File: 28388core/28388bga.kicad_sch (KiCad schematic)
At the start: 131 parts, among them IC1 F28388DZWTS, IC2 TPS62420DRCT, IC6 OPA4350EA_250, IC7 TPS3702CX33DDCT, IC8 CDCLVC1104PW, J4 Conn_02x10_Top_Bottom, J6 2.54-2*5, J9 Conn_02x07_Odd_Even, M1 Conn_01x01_Socket, M2 Conn_01x01_Socket, M3 Conn_01x01_Socket, M4 Conn_01x01_Socket, M5 Conn_01x01_Socket, M6 Conn_01x01_Socket, M7 Conn_01x01_Socket, Q1 FMMT618TA, Q11 AT24C16C-SSHM-T, Q2 FMMT618TA, Q4 FMMT618TA, Q7 FMMT618TA, SW1 SW_DIP_x02, SW2 SW_Push, U1 ADR423ARMZ, Y1 ECS-2520S33-250-FN-TR

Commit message: 第一版引脚分配
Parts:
- removed C216, C218: 0.1uF/50V, Capacitor_SMD:C_0603_1608Metric, symbol sheet1-altium-import:CAP_2
- removed C217, C219: 10uF/50V, Capacitor_SMD:C_0603_1608Metric, symbol sheet1-altium-import:CAP_2
- removed J4: Conn_02x10_Top_Bottom, Connector_PinHeader_2.54mm:PinHeader_2x10_P2.54mm_Vertical, symbol Connector_Generic:Conn_02x10_Top_Bottom
- removed M1, M2, M3, M4, M5, M6, M7: Conn_01x01_Socket, 1mmlab_footprint:M3, symbol Connector:Conn_01x01_Socket
- added CARD2: DDR3, 1mmlab_footprint:PCBComponent_1 - duplicate, symbol 1mmlab:DDR3
- added D45: SK36A-LTP, Lib_sheet_10:SMA_L4.3-W2.6-LS5.2-RD, symbol sheet1-altium-import:SK36A-LTP
- added H1, H2: MountingHole_Pad, MountingHole:MountingHole_2.2mm_M2_Pad_Via, symbol Mechanical:MountingHole_Pad
- added Q46: TYPEC-304-ACP16, Lib4:USB-C-SMD_TYPE-C-16P-1, symbol sheet1-altium-import:TYPEC-304-ACP16
- added R301, R302: 4.7K/1%, Resistor_SMD:R_0603_1608Metric, symbol sheet1-altium-import:RES_4
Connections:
- net ADC_14_IN: now also CARD2.19
- net ADC_15_IN: now also CARD2.21
- net ADC_A0_IN: now also CARD2.3
- net ADC_A1_IN: now also CARD2.5
- net ADC_A2_IN: now also CARD2.9
- net ADC_A3_IN: now also CARD2.11
- net ADC_A4_IN: now also CARD2.15
- net ADC_A5_IN: now also CARD2.17
- net ADC_B0_IN: now also CARD2.4
- net ADC_B1_IN: now also CARD2.6
- net ADC_B2_IN: now also CARD2.10
- net ADC_B3_IN: now also CARD2.12
- net ADC_B4_IN: now also CARD2.16
- net ADC_B5_IN: now also CARD2.18
- net ADC_C2_IN: now also CARD2.25
- net ADC_C3_IN: now also CARD2.27
- net ADC_C4_IN: now also CARD2.31
- net ADC_C5_IN: now also CARD2.33
- net ADC_D0_IN: now also CARD2.20
- net ADC_D1_IN: now also CARD2.22
- net ADC_D2_IN: now also CARD2.26
- net ADC_D3_IN: now also CARD2.28
- net ADC_D4_IN: now also CARD2.32
- net ADC_D5_IN: now also CARD2.34
- net D+5V: now also D45.1 (K)
- net DSP_GPIO145: now also D10.2 (K), R39.2
- net DSP_GPIO146: now also D11.1 (K), R40.2
- net DSP_GPIO150: now also Q11.5 (SDA), R34.1
- net DSP_GPIO151: now also Q11.6 (SCL), R33.1
- net DSP_GPIO40: no longer Q11.5 (SDA), R34.1
- net DSP_GPIO41: no longer Q11.6 (SCL), R33.1
- net DSP_GPIO60: no longer D10.2 (K), R39.2
- net DSP_GPIO61: no longer D11.1 (K), R40.2
- net PE_GND: now also H1.1, H2.1
- new net: Q46.B5 (CC2), R302.2
- new net: Q46.A5 (CC1), R301.1
- new net AGND: Q46.A1B12 (GND), Q46.B1A12 (GND), R301.2, R302.1
- new net GPIO0: CARD2.47
- new net GPIO1: CARD2.49
- new net GPIO10: CARD2.61
- new net GPIO100: CARD2.173
- new net GPIO101: CARD2.175
- new net GPIO102: CARD2.166
- new net GPIO103: CARD2.168
- new net GPIO104: CARD2.170
- new net GPIO105: CARD2.172
- new net GPIO106: CARD2.174
- new net GPIO107: CARD2.176
- new net GPIO108: CARD2.179
- new net GPIO109: CARD2.181
- new net GPIO11: CARD2.63
- new net GPIO110: CARD2.183
- new net GPIO111: CARD2.185
- new net GPIO112: CARD2.187
- new net GPIO115: CARD2.180
- new net GPIO116: CARD2.182
- new net GPIO117: CARD2.184
- new net GPIO119: CARD2.186
- new net GPIO12: CARD2.58
- new net GPIO120: CARD2.188
- new net GPIO121: CARD2.191
- new net GPIO122: CARD2.193
- new net GPIO123: CARD2.195
- new net GPIO124: CARD2.197
- new net GPIO126: CARD2.192
- new net GPIO127: CARD2.194
- new net GPIO128: CARD2.196
- new net GPIO13: CARD2.60
- new net GPIO14: CARD2.62
- new net GPIO147: CARD2.198
- new net GPIO15: CARD2.64
- new net GPIO154: CARD2.200
- new net GPIO16: CARD2.67
- new net GPIO17: CARD2.69
- new net GPIO18: CARD2.68
- new net GPIO19: CARD2.70
- new net GPIO2: CARD2.51
- new net GPIO20: CARD2.77
- new net GPIO21: CARD2.79
- new net GPIO22: CARD2.81
- new net GPIO23: CARD2.83
- new net GPIO24: CARD2.85
- new net GPIO25: CARD2.87
- new net GPIO26: CARD2.78
- new net GPIO27: CARD2.80
- new net GPIO28: CARD2.82
- new net GPIO29: CARD2.84
- new net GPIO3: CARD2.53
- new net GPIO30: CARD2.86
- new net GPIO31: CARD2.88
- new net GPIO32: CARD2.91
- new net GPIO33: CARD2.93
- new net GPIO34: CARD2.95
- new net GPIO35: CARD2.97
- new net GPIO36: CARD2.99
- new net GPIO37: CARD2.101
- new net GPIO38: CARD2.92
- new net GPIO39: CARD2.94
- new net GPIO4: CARD2.48
- new net GPIO40: CARD2.96
- new net GPIO41: CARD2.98
- new net GPIO42: CARD2.100
- new net GPIO43: CARD2.102
- new net GPIO44: CARD2.105
- new net GPIO45: CARD2.107
- new net GPIO46: CARD2.109
- new net GPIO47: CARD2.111
- new net GPIO48: CARD2.113
- new net GPIO49: CARD2.115
- new net GPIO5: CARD2.50
- new net GPIO50: CARD2.106
- new net GPIO51: CARD2.108
- new net GPIO52: CARD2.110
- new net GPIO53: CARD2.112
- new net GPIO54: CARD2.114
- new net GPIO55: CARD2.116
- new net GPIO56: CARD2.119
- new net GPIO57: CARD2.121
- new net GPIO58: CARD2.123
- new net GPIO59: CARD2.125
- new net GPIO6: CARD2.52
- new net GPIO60: CARD2.127
- new net GPIO61: CARD2.129
- new net GPIO62: CARD2.120
- new net GPIO63: CARD2.122
- new net GPIO64: CARD2.124
- new net GPIO65: CARD2.126
- new net GPIO66: CARD2.128
- new net GPIO67: CARD2.130
- new net GPIO68: CARD2.133
- new net GPIO69: CARD2.135
- new net GPIO7: CARD2.54
- new net GPIO70: CARD2.137
- new net GPIO71: CARD2.139
- new net GPIO72: CARD2.141
- new net GPIO73: CARD2.143
- new net GPIO74: CARD2.134
- new net GPIO75: CARD2.136
- new net GPIO76: CARD2.138
- new net GPIO77: CARD2.140
- new net GPIO78: CARD2.142
- new net GPIO79: CARD2.144
- new net GPIO8: CARD2.57
- new net GPIO80: CARD2.147
- new net GPIO81: CARD2.149
- new net GPIO82: CARD2.151
- new net GPIO83: CARD2.153
- new net GPIO84: CARD2.155
- new net GPIO85: CARD2.157
- new net GPIO86: CARD2.159
- new net GPIO87: CARD2.161
- new net GPIO88: CARD2.148
- new net GPIO89: CARD2.150
- new net GPIO9: CARD2.59
- new net GPIO90: CARD2.152
- new net GPIO91: CARD2.154
- new net GPIO92: CARD2.156
- new net GPIO93: CARD2.158
- new net GPIO94: CARD2.160
- new net GPIO95: CARD2.162
- new net GPIO96: CARD2.165
- new net GPIO97: CARD2.167
- new net GPIO98: CARD2.169
- new net GPIO99: CARD2.171
- new net USB_D+5V: D45.2 (A), Q46.A4B9 (VBUS), Q46.B4A9 (VBUS)
- no-connect marks 12 -> 18
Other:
- note added: "5V type-c power input"
- note removed: "ADCExtension"
- note removed: "DSP的ADC保护靠近DSP，不用管外接口"
- moved on the sheet: C215, D18, R345, R366

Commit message: 添加封装和完成引脚配对
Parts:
- removed J6: 2.54-2*5, Lib_sheet_10:HDR-TH_10P-P2.54-V-F-R2-C5-S2.54, symbol sheet1-altium-import:2.54-2*5_2
- added J1: Conn_01x02, 1mmlab_footprint:CONN-TH_2P-P2.54_DIBO_DB141R-2.54-2P, symbol Connector_Generic:Conn_01x02
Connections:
- net DSP_GPIO0 is gone; now on net GPIO0: IC1.C8 (GPIO0)
- net DSP_GPIO1 is gone; now on net GPIO1: IC1.D8 (GPIO1)
- net DSP_GPIO10 is gone; now on net GPIO10: IC1.B2 (GPIO10)
- net DSP_GPIO100 is gone; now on net GPIO100: IC1.H1 (GPIO100)
- net DSP_GPIO101 is gone; now on net GPIO101: IC1.H2 (GPIO101)
- net DSP_GPIO102 is gone; now on net GPIO102: IC1.H3 (GPIO102)
- net DSP_GPIO103 is gone; now on net GPIO103: IC1.J1 (GPIO103)
- net DSP_GPIO104 is gone; now on net GPIO104: IC1.J2 (GPIO104)
- net DSP_GPIO105 is gone; now on net GPIO105: IC1.J3 (GPIO105)
- net DSP_GPIO106 is gone; now on net GPIO106: IC1.L2 (GPIO106)
- net DSP_GPIO107 is gone; now on net GPIO107: IC1.L3 (GPIO107)
- net DSP_GPIO108 is gone; now on net GPIO108: IC1.L4 (GPIO108)
- net DSP_GPIO109 is gone; now on net GPIO109: IC1.N2 (GPIO109)
- net DSP_GPIO11 is gone; now on net GPIO11: IC1.C1 (GPIO11)
- net DSP_GPIO110 is gone; now on net GPIO110: IC1.M2 (GPIO110)
- net DSP_GPIO111 is gone; now on net GPIO111: IC1.M4 (GPIO111)
- net DSP_GPIO112 is gone; now on net GPIO112: IC1.M3 (GPIO112)
- net DSP_GPIO115 is gone; now on net GPIO115: IC1.V12 (GPIO115)
- net DSP_GPIO116 is gone; now on net GPIO116: IC1.W10 (GPIO116)
- net DSP_GPIO117 is gone; now on net GPIO117: IC1.U12 (GPIO117)
- net DSP_GPIO119 is gone; now on net GPIO119: IC1.T15 (GPIO119)
- net DSP_GPIO12 is gone; now on net GPIO12: IC1.C2 (GPIO12)
- net DSP_GPIO120 is gone; now on net GPIO120: IC1.U15 (GPIO120)
- net DSP_GPIO121 is gone; now on net GPIO121: IC1.W16 (GPIO121)
- net DSP_GPIO122 is gone; now on net GPIO122: IC1.T8 (GPIO122)
- net DSP_GPIO123 is gone; now on net GPIO123: IC1.U8 (GPIO123)
- net DSP_GPIO124 is gone; now on net GPIO124: IC1.V8 (GPIO124)
- net DSP_GPIO126 is gone; now on net GPIO126: IC1.U9 (GPIO126)
- net DSP_GPIO127 is gone; now on net GPIO127: IC1.V9 (GPIO127)
- net DSP_GPIO128 is gone; now on net GPIO128: IC1.W9 (GPIO128)
- net DSP_GPIO13 is gone; now on net GPIO13: IC1.D1 (GPIO13)
- net DSP_GPIO14 is gone; now on net GPIO14: IC1.D2 (GPIO14)
- net DSP_GPIO147 is gone; now on net GPIO147: IC1.D17 (GPIO147)
- net DSP_GPIO15 is gone; now on net GPIO15: IC1.D3 (GPIO15)
- net DSP_GPIO154 is gone; now on net GPIO154: IC1.B12 (GPIO154)
- net DSP_GPIO16 is gone; now on net GPIO16: IC1.E1 (GPIO16)
- net DSP_GPIO17 is gone; now on net GPIO17: IC1.E2 (GPIO17)
- net DSP_GPIO18 is gone; now on net GPIO18: IC1.E3 (GPIO18)
- net DSP_GPIO19 is gone; now on net GPIO19: IC1.E4 (GPIO19)
- net DSP_GPIO2 is gone; now on net GPIO2: IC1.A7 (GPIO2)
- net DSP_GPIO20 is gone; now on net GPIO20: IC1.F2 (GPIO20)
- net DSP_GPIO21 is gone; now on net GPIO21: IC1.F3 (GPIO21)
- net DSP_GPIO22 is gone; now on net GPIO22: IC1.J4 (GPIO22)
- net DSP_GPIO23 is gone; now on net GPIO23: IC1.K4 (GPIO23)
- net DSP_GPIO24 is gone; now on net GPIO24: IC1.K3 (GPIO24)
- net DSP_GPIO25 is gone; now on net GPIO25: IC1.K2 (GPIO25)
- net DSP_GPIO26 is gone; now on net GPIO26: IC1.K1 (GPIO26)
- net DSP_GPIO27 is gone; now on net GPIO27: IC1.L1 (GPIO27)
- net DSP_GPIO28 is gone; now on net GPIO28: IC1.V11 (GPIO28)
- net DSP_GPIO29 is gone; now on net GPIO29: IC1.W11 (GPIO29)
- net DSP_GPIO3 is gone; now on net GPIO3: IC1.B7 (GPIO3)
- net DSP_GPIO30 is gone; now on net GPIO30: IC1.T11 (GPIO30)
- net DSP_GPIO31 is gone; now on net GPIO31: IC1.U11 (GPIO31)
- net DSP_GPIO32 is gone; now on net GPIO32: IC1.U13 (GPIO32)
- net DSP_GPIO33 is gone; now on net GPIO33: IC1.T13 (GPIO33)
- net DSP_GPIO34 is gone; now on net GPIO34: IC1.U14 (GPIO34)
- net DSP_GPIO35 is gone; now on net GPIO35: IC1.T14 (GPIO35)
- net DSP_GPIO36 is gone; now on net GPIO36: IC1.V16 (GPIO36)
- net DSP_GPIO37 is gone; now on net GPIO37: IC1.U16 (GPIO37)
- net DSP_GPIO38 is gone; now on net GPIO38: IC1.T16 (GPIO38)
- net DSP_GPIO39 is gone; now on net GPIO39: IC1.W17 (GPIO39)
- net DSP_GPIO4 is gone; now on net GPIO4: IC1.C7 (GPIO4)
- net DSP_GPIO40 is gone; now on net GPIO40: IC1.V17 (GPIO40)
- net DSP_GPIO41 is gone; now on net GPIO41: IC1.U17 (GPIO41)
- net DSP_GPIO42 is gone; now on net GPIO42: IC1.D19 (GPIO42)
- net DSP_GPIO43 is gone; now on net GPIO43: IC1.C19 (GPIO43)
- net DSP_GPIO44 is gone; now on net GPIO44: IC1.K18 (GPIO44)
- net DSP_GPIO45 is gone; now on net GPIO45: IC1.K19 (GPIO45)
- net DSP_GPIO46 is gone; now on net GPIO46: IC1.E19 (GPIO46)
- net DSP_GPIO47 is gone; now on net GPIO47: IC1.E18 (GPIO47)
- net DSP_GPIO48 is gone; now on net GPIO48: IC1.R16 (GPIO48)
- net DSP_GPIO49 is gone; now on net GPIO49: IC1.R17 (GPIO49)
- net DSP_GPIO5 is gone; now on net GPIO5: IC1.D7 (GPIO5)
- net DSP_GPIO50 is gone; now on net GPIO50: IC1.R18 (GPIO50)
- net DSP_GPIO51 is gone; now on net GPIO51: IC1.R19 (GPIO51)
- net DSP_GPIO52 is gone; now on net GPIO52: IC1.P16 (GPIO52)
- net DSP_GPIO53 is gone; now on net GPIO53: IC1.P17 (GPIO53)
- net DSP_GPIO54 is gone; now on net GPIO54: IC1.P18 (GPIO54)
- net DSP_GPIO55 is gone; now on net GPIO55: IC1.P19 (GPIO55)
- net DSP_GPIO56 is gone; now on net GPIO56: IC1.N16 (GPIO56)
- net DSP_GPIO57 is gone; now on net GPIO57: IC1.N18 (GPIO57)
- net DSP_GPIO58 is gone; now on net GPIO58: IC1.N17 (GPIO58)
- net DSP_GPIO59 is gone; now on net GPIO59: IC1.M16 (GPIO59)
- net DSP_GPIO6 is gone; now on net GPIO6: IC1.A6 (GPIO6)
- net DSP_GPIO60 is gone; now on net GPIO60: IC1.M17 (GPIO60)
- net DSP_GPIO61 is gone; now on net GPIO61: IC1.L16 (GPIO61)
- net DSP_GPIO62 is gone; now on net GPIO62: IC1.J17 (GPIO62)
- net DSP_GPIO63 is gone; now on net GPIO63: IC1.J16 (GPIO63)
- net DSP_GPIO64 is gone; now on net GPIO64: IC1.L17 (GPIO64)
- net DSP_GPIO65 is gone; now on net GPIO65: IC1.K16 (GPIO65)
- net DSP_GPIO66 is gone; now on net GPIO66: IC1.K17 (GPIO66)
- net DSP_GPIO67 is gone; now on net GPIO67: IC1.B19 (GPIO67)
- net DSP_GPIO68 is gone; now on net GPIO68: IC1.C18 (GPIO68)
- net DSP_GPIO69 is gone; now on net GPIO69: IC1.B18 (GPIO69)
- net DSP_GPIO7 is gone; now on net GPIO7: IC1.B6 (GPIO7)
- net DSP_GPIO70 is gone; now on net GPIO70: IC1.A17 (GPIO70)
- net DSP_GPIO71 is gone; now on net GPIO71: IC1.B17 (GPIO71)
- net DSP_GPIO72 is gone; now on net GPIO72: IC1.B16 (GPIO72), R49.2, SW1.1
- net DSP_GPIO73 is gone; now on net GPIO73: IC1.A16 (GPIO73)
- net DSP_GPIO74 is gone; now on net GPIO74: IC1.C17 (GPIO74)
- net DSP_GPIO75 is gone; now on net GPIO75: IC1.D16 (GPIO75)
- net DSP_GPIO76 is gone; now on net GPIO76: IC1.C16 (GPIO76)
- net DSP_GPIO77 is gone; now on net GPIO77: IC1.A15 (GPIO77)
- net DSP_GPIO78 is gone; now on net GPIO78: IC1.B15 (GPIO78)
- net DSP_GPIO79 is gone; now on net GPIO79: IC1.C15 (GPIO79)
- net DSP_GPIO8 is gone; now on net GPIO8: IC1.G2 (GPIO8)
- net DSP_GPIO80 is gone; now on net GPIO80: IC1.D15 (GPIO80)
- net DSP_GPIO81 is gone; now on net GPIO81: IC1.A14 (GPIO81)
- net DSP_GPIO82 is gone; now on net GPIO82: IC1.B14 (GPIO82)
- net DSP_GPIO83 is gone; now on net GPIO83: IC1.C14 (GPIO83)
- net DSP_GPIO84 is gone; now on net GPIO84: IC1.A11 (GPIO84), R47.2, SW1.2
- net DSP_GPIO85 is gone; now on net GPIO85: IC1.B11 (GPIO85)
- net DSP_GPIO86 is gone; now on net GPIO86: IC1.C11 (GPIO86)
- net DSP_GPIO87 is gone; now on net GPIO87: IC1.D11 (GPIO87)
- net DSP_GPIO88 is gone; now on net GPIO88: IC1.C6 (GPIO88)
- net DSP_GPIO89 is gone; now on net GPIO89: IC1.D6 (GPIO89)
- net DSP_GPIO9 is gone; now on net GPIO9: IC1.G3 (GPIO9)
- net DSP_GPIO90 is gone; now on net GPIO90: IC1.A5 (GPIO90)
- net DSP_GPIO91 is gone; now on net GPIO91: IC1.B5 (GPIO91)
- net DSP_GPIO92 is gone; now on net GPIO92: IC1.A4 (GPIO92)
- net DSP_GPIO93 is gone; now on net GPIO93: IC1.B4 (GPIO93)
- net DSP_GPIO94 is gone; now on net GPIO94: IC1.A3 (GPIO94)
- net DSP_GPIO95 is gone; now on net GPIO95: IC1.B3 (GPIO95)
- net DSP_GPIO96 is gone; now on net GPIO96: IC1.C3 (GPIO96)
- net DSP_GPIO97 is gone; now on net GPIO97: IC1.A2 (DSP_97)
- net DSP_GPIO98 is gone; now on net GPIO98: IC1.F1 (GPIO98)
- net DSP_GPIO99 is gone; now on net GPIO99: IC1.G1 (GPIO99)
- net D+5V: now also CARD2.104, CARD2.118, CARD2.132, CARD2.146, CARD2.164, CARD2.178, CARD2.190, CARD2.204, CARD2.74, CARD2.76, CARD2.90, J1.1 (Pin_1)
- net GND: now also CARD2.1, CARD2.103, CARD2.117, CARD2.13, CARD2.131, CARD2.14, CARD2.145, CARD2.163, CARD2.177, CARD2.189, CARD2.2, CARD2.203, CARD2.23, CARD2.24, CARD2.29, CARD2.30, CARD2.35, CARD2.36, CARD2.45, CARD2.46, CARD2.55, CARD2.56, CARD2.65, CARD2.66, CARD2.7, CARD2.71, CARD2.72, CARD2.73, CARD2.75, CARD2.8, CARD2.89, J1.2 (Pin_2)
- net DSP_GPIO113 renamed GPIO113
- net DSP_GPIO114 renamed GPIO114
- net DSP_GPIO118 renamed GPIO118
- net DSP_GPIO125 renamed GPIO125
- net DSP_GPIO129 renamed ESC_TX1_EN
- net DSP_GPIO130 renamed ESC_TX1_CLK
- net DSP_GPIO131 renamed ESC_TX1_D0
- net DSP_GPIO132 renamed ESC_TX1_D1
- net DSP_GPIO133 renamed GPIO133
- net DSP_GPIO134 renamed ESC_TX1_D2
- net DSP_GPIO135 renamed ESC_TX1_D3
- net DSP_GPIO136 renamed ESC_RX1_DV
- net DSP_GPIO137 renamed ESC_RX1_CLK
- net DSP_GPIO138 renamed ESC_RX1_ERR
- net DSP_GPIO139 renamed ESC_RX1_D0
- net DSP_GPIO140 renamed ESC_RX1_D1
- net DSP_GPIO141 renamed ESC_RX1_D2
- net DSP_GPIO142 renamed ESC_RX1_D3
- net DSP_GPIO143 renamed ESC_LED_LINK0
- net DSP_GPIO144 renamed ESC_LED_LINK1
- net DSP_GPIO145 renamed ESC_LED_ERR
- net DSP_GPIO146 renamed ESC_LED_RUN
- net DSP_GPIO148 renamed ESC_PHY0
- net DSP_GPIO149 renamed ESC_PHY1
- net DSP_GPIO150 renamed ESC_I2C_SDA
- net DSP_GPIO151 renamed ESC_I2C_SCL
- net DSP_GPIO152 renamed ESC_MDC
- net DSP_GPIO153 renamed ESC_MDIO
- net DSP_GPIO155 renamed ESC_RESET
- net DSP_GPIO156 renamed ESC_TX0_EN
- net DSP_GPIO157 renamed ESC_TX0_CLK
- net DSP_GPIO158 renamed ESC_TX0_D0
- net DSP_GPIO159 renamed ESC_TX0_D1
- net DSP_GPIO160 renamed ESC_TX0_D2
- net DSP_GPIO161 renamed ESC_TX0_D3
- net DSP_GPIO162 renamed ESC_RX0_DV
- net DSP_GPIO163 renamed ESC_RX0_CLK
- net DSP_GPIO164 renamed ESC_RX0_ERR
- net DSP_GPIO165 renamed ESC_RX0_D0
- net DSP_GPIO166 renamed ESC_RX0_D1
- net DSP_GPIO167 renamed ESC_RX0_D2
- net DSP_GPIO168 renamed ESC_RX0_D3
- no-connect marks 18 -> 29

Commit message: 添加Voltage Monitoring
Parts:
- removed D18: DNP, Diode_SMD:D_SMC, symbol Device:D_TVS
- added C50: 0.01uF, Capacitor_SMD:C_0402_1005Metric, symbol Device:C_Small
- added C72: 0.1uF, Capacitor_SMD:C_0402_1005Metric, symbol Device:C_Small
- added IC9: TPS3702CX12DDCT, SamacSys_Parts:SOT95P280X110-6N, symbol SamacSys_Parts:TPS3702CX33DDCT
- added R107, R108: DNP, Resistor_SMD:R_0402_1005Metric, symbol Device:R_Small
- added R109: 2.2k, Resistor_SMD:R_0402_1005Metric, symbol Device:R_Small
- C46: value 0.1uF -> 0.01uF
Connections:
- net +1V2_DSP: now also IC9.3 (SENSE)
- net +3V3D_DSP: now also C72.1, IC9.4 (SET), IC9.5 (VDD), R109.2
- net DSP_XRSn: now also IC9.1 (UV)
- net GND: now also C50.2, C72.2, IC9.2 (GND), R107.2
- net GPIO107: now also R108.2
- net at IC7.6 (OV): now also C50.1, IC9.6 (OV), R108.1, R109.1
- net at Y1.1 (TRI-STATE): now also R107.1
- no-connect marks 29 -> 27
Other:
- moved on the sheet: C16, C215, C242, C243, C29, C31, C32, C33, C34, C37, C38, C39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

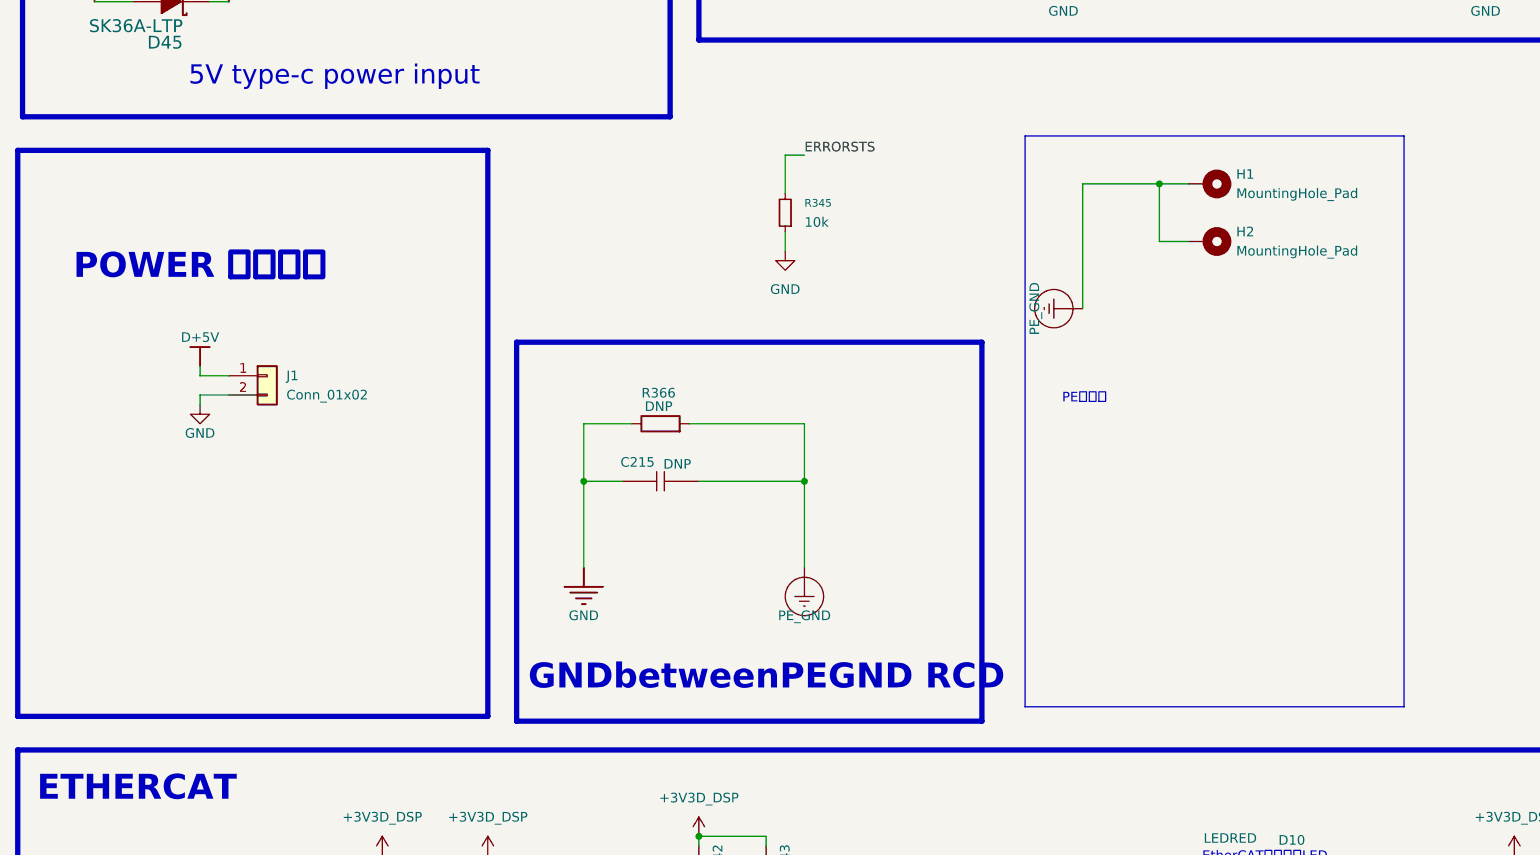
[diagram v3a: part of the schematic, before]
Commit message: 只保留type-c接口供电
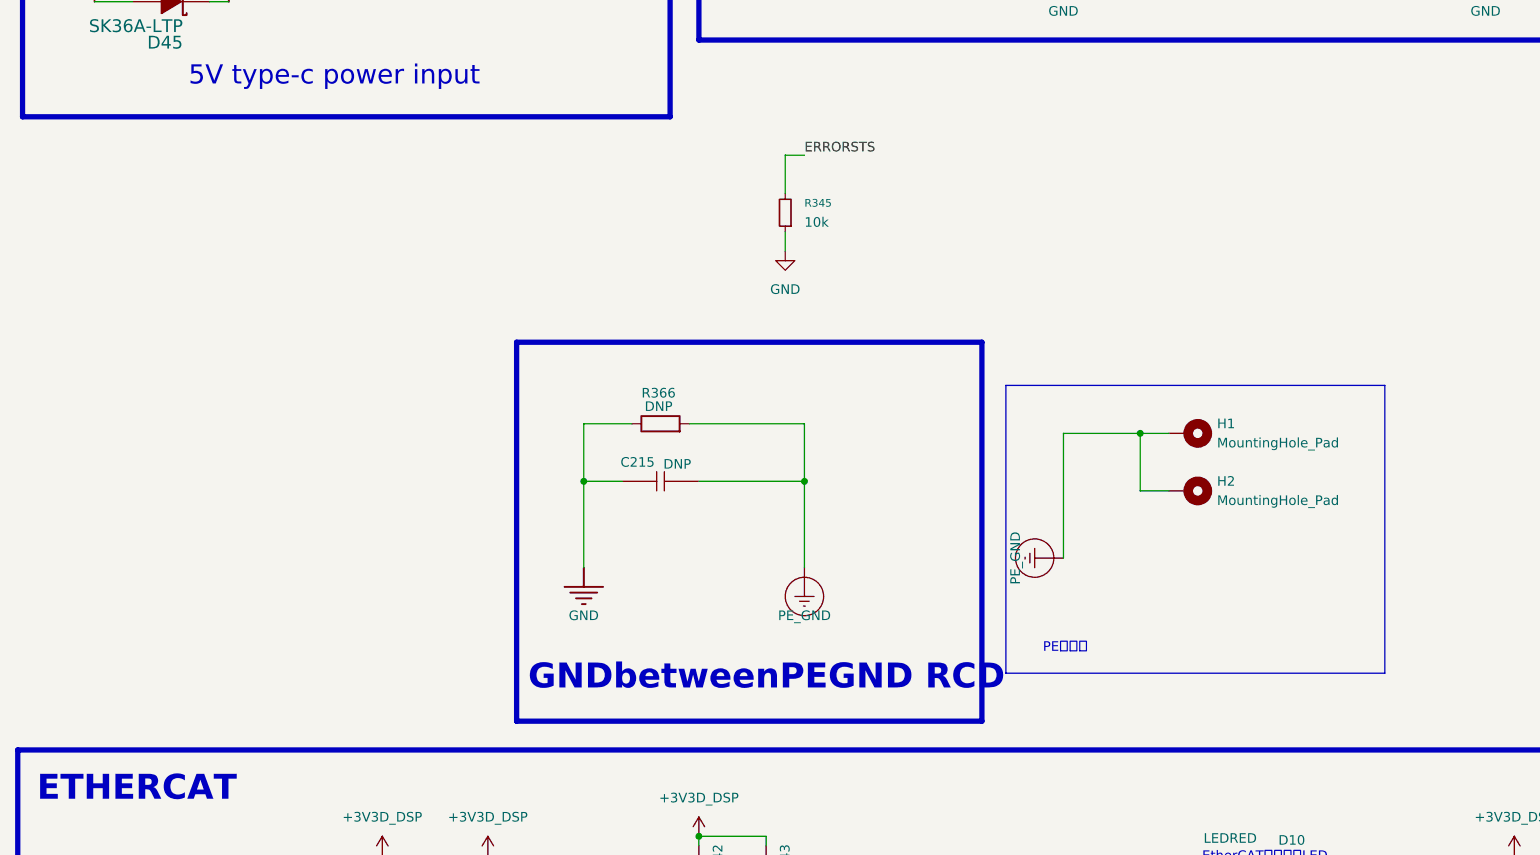
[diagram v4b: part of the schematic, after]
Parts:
- removed J1: Conn_01x02, 1mmlab_footprint:CONN-TH_2P-P2.54_DIBO_DB141R-2.54-2P, symbol Connector_Generic:Conn_01x02
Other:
- note removed: "POWER 电源进！"
- moved on the sheet: H1, H2
